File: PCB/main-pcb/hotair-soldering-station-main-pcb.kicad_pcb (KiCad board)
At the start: 2 copper layers, 89.4 x 90.9 mm, 89 parts, among them J1 230VAC_IN, J10 PB6, J11 PB4, J12 PB7, J13 ICP (goldpin r2,54), J2 main-board-conn, J3 EARTH_GND, J4 24V_IN (NS-25 r2,54), J5 PSUPPLY (PWZ-02S r.3,96), J6 HOTAIR_FAN (JST r,2,54)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

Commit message: LED display, buzzer and PWM done in SW. Some HW bugs fixed.
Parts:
- added D7: 1N4148, Diodes_SMD:D_MiniMELF, F.Cu at (27.2, 104.6)
- added R11: 2k, Capacitors:0805, B.Cu at (28.3, 95.6)
- moved Q9 2.88 mm to (30.4, 106.0)
- moved R31 2.54 mm to (33.8, 107.1)
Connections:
- LS1 pad +: Net-(LS1-Pad+) -> Net-(D7-Pad2)
- Q9 pad 3: Net-(LS1-Pad+) -> Net-(D7-Pad1)
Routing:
- net Net-(D7-Pad2): track 0.00 -> 16.4 mm
- net Net-(LS1-Pad+): track 11.0 -> 0.00 mm
- net +5V: track 144.5 -> 149.0 mm
- net BUZZER: track 61.1 -> 58.8 mm
- net Net-(D7-Pad1): track 0.00 -> 2.19 mm
- net Net-(Q9-Pad1): track 2.19 -> 1.56 mm

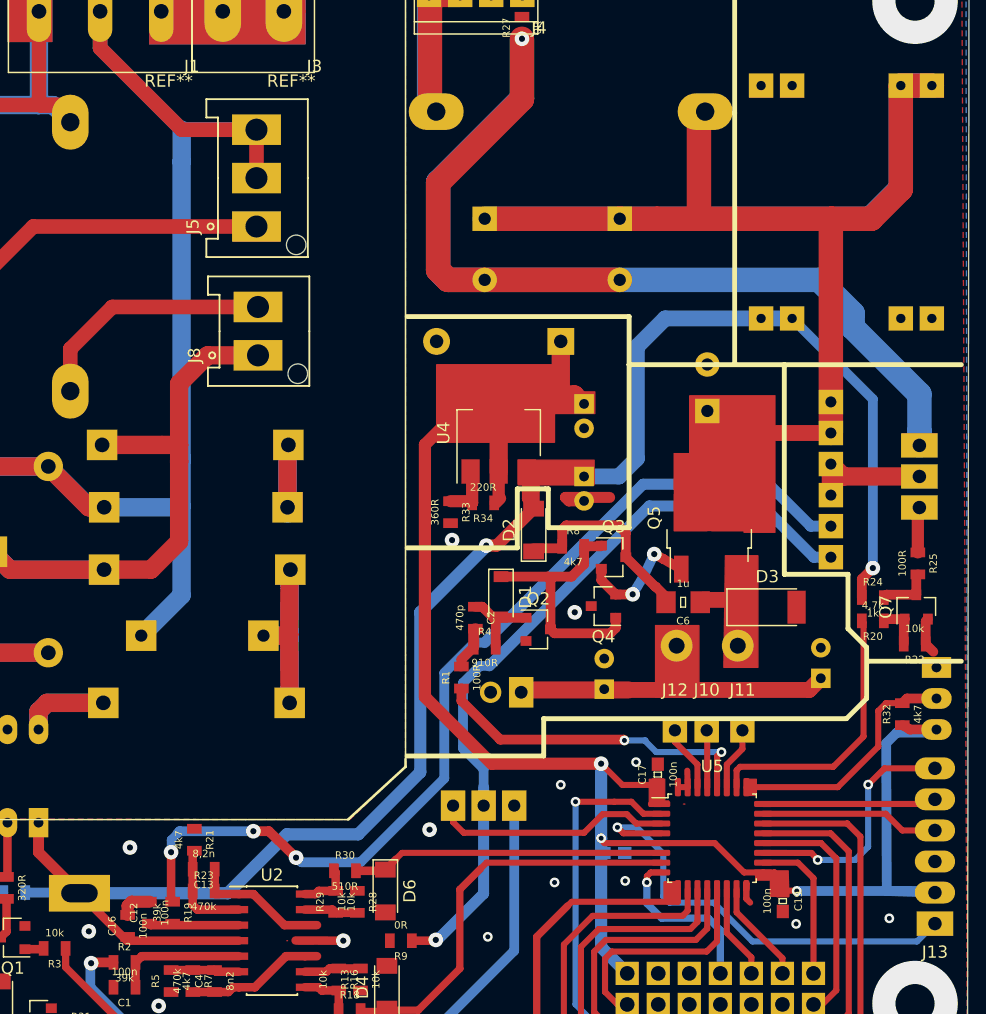
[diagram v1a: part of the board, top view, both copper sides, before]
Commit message: Fan DC converter new design, ADC and PWM done
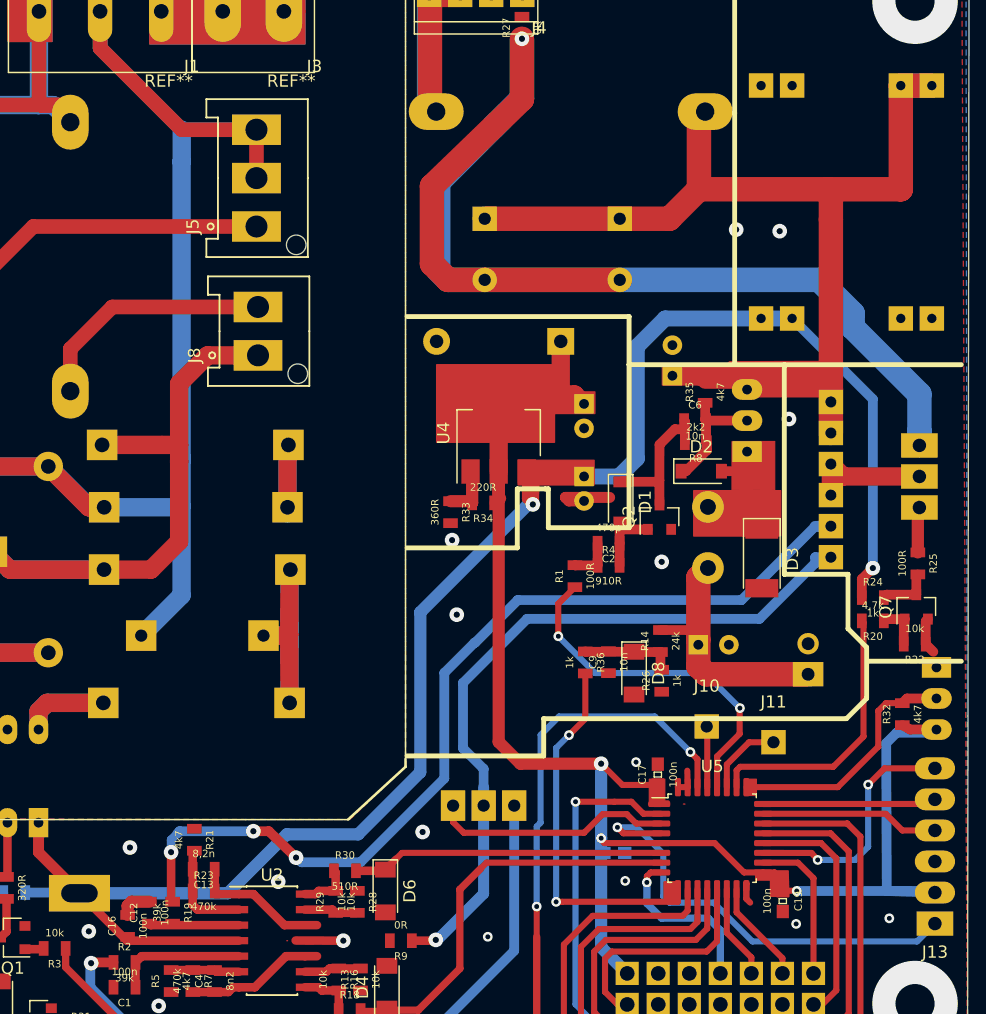
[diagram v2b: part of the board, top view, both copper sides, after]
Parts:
- removed J12: PB7, My-Footprints:WIRE_PAD_1,3mm
- removed Q4: BC807, Package_TO_SOT_SMD:SOT-23
- removed Q5: IRLIZ44N, TO_SOT_Packages_SMD:TO-252-2
- added D8: 3V6, Diodes_SMD:D_MiniMELF, F.Cu at (79.0, 77.7)
- added R14: 24k, Capacitors:0805, F.Cu at (81.2, 75.1)
- added R26: 1k, Capacitors:0805, F.Cu at (81.3, 78.3)
- added R35: 4k7, Capacitors:0805, F.Cu at (84.8, 54.7)
- added R36: 1k, Capacitors:0805, F.Cu at (75.0, 76.8)
- C3: footprint Capacitor_THT:CP_Radial_D10.0mm_P3.80mm -> Capacitor_THT:CP_Radial_D6.3mm_P2.50mm
- C6: value 1u -> 10n; footprint Capacitors:1206 -> Capacitors:0805
- C9: value 47u/35V -> 10n; footprint Capacitor_THT:CP_Radial_D6.3mm_P2.50mm -> Capacitors:0805; moved to F.Cu
- D2: value 1N4148 -> MBR052; footprint Diodes_SMD:D_MiniMELF -> Diodes_SMD:D_SOD-123
- Q3: value BC817 -> BC327; footprint Package_TO_SOT_SMD:SOT-23 -> My-Footprints:TO-92_Inline_Wide; moved to B.Cu
- R8: value 4k7 -> 2k2
- moved J6 23.5 mm to (93.3, 77.8), turned to 90 degrees
- moved C9 17.4 mm to (76.9, 76.8)
- moved C6 14.9 mm to (84.0, 57.0), turned to 0 degrees
- moved D2 14.5 mm to (84.5, 61.2), turned to 0 degrees
- moved Q3 13.9 mm to (88.3, 59.6), turned to 90 degrees
- moved Q2 13.5 mm to (81.1, 64.9), turned to 90 degrees
- moved R8 13.1 mm to (84.1, 58.8), turned to 180 degrees
- moved D1 12.5 mm to (77.9, 63.7)
- moved C2 12.5 mm to (76.9, 67.1), turned to 180 degrees
- moved R1 12.4 mm to (74.2, 69.7)
- moved R4 12.1 mm to (76.9, 68.9)
- moved L1 11.6 mm to (85.1, 64.1), turned to 270 degrees
- moved C8 8.51 mm to (84.3, 75.4), turned to 0 degrees
- moved C3 4.06 mm to (82.2, 53.4)
- moved D3 3.97 mm to (89.5, 68.3), turned to 270 degrees
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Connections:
- C9 pad 1: FAN_SUPPLY -> GND
- C9 pad 2: GND -> Net-(C9-Pad2)
- D1 pad 1: Net-(D1-Pad1) -> Net-(C6-Pad1)
- D2 pad 2: +5V -> Net-(D2-Pad2)
- D3 pad 1: Net-(C6-Pad1) -> Net-(D2-Pad2)
- L1 pad 1: Net-(C6-Pad1) -> Net-(D2-Pad2)
- Q2 pad 3: Net-(D1-Pad1) -> Net-(C6-Pad1)
- Q3 pad 1: Net-(D1-Pad1) -> Net-(D2-Pad2)
- Q3 pad 2: Net-(Q3-Pad2) -> Net-(C6-Pad2)
- Q3 pad 3: Net-(C6-Pad2) -> +24V
- R8 pad 2: Net-(D1-Pad1) -> Net-(C6-Pad1)
- U5 pad 30: Net-(J12-Pad1) -> HOTAIR_HEATER_CTRL
- U5 pad 9: HOTAIR_HEATER_CTRL -> FAN_ADC
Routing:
- net +24V: track 134.8 -> 88.1 mm
- net FAN_ADC: track 0.00 -> 31.9 mm, vias 0 -> 2
- net Net-(D1-Pad1): track 21.0 -> 0.00 mm
- net HOTAIR_HEATER_CTRL: track 62.9 -> 83.0 mm, vias 0 -> 2
- net Net-(D2-Pad2): track 0.00 -> 16.7 mm
- net +3V3: track 143.7 -> 131.8 mm
- net Net-(Q3-Pad2): track 11.4 -> 0.00 mm, vias 2 -> 0
- net Net-(C9-Pad2): track 0.00 -> 7.66 mm
- net FAN_SUPPLY: track 28.5 -> 21.0 mm
- net Net-(C6-Pad2): track 16.4 -> 10.1 mm
- net Net-(J12-Pad1): track 5.42 -> 0.00 mm
- net Net-(C6-Pad1): track 9.25 -> 12.6 mm
- net SOLDERING_IRON_THERM: track 79.7 -> 76.8 mm
- net THERM_GND: track 64.8 -> 62.3 mm
- net FAN_PWM: track 27.1 -> 29.1 mm
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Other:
- net class gnd added: clearance 0.7, trace_width 2, via_dia 0.8, via_drill 0.4
